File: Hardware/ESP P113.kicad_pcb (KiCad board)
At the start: 2 copper layers, 104.8 x 73.7 mm, 55 parts, among them J1 L_In, J2 R_In, J3 L_Out, J4 R_Out, J5 AC_In, Q1 MJE15032, Q2 MJE15033, Q3 MJE15032, Q4 MJE15033, U1 LM4562

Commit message: Updated to V1.1
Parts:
- added F1: Fuse_Small, Fuse:Fuseholder_Cylinder-5x20mm_Schurter_0031_8201_Horizontal_Open, F.Cu at (74.9, 62.2)
- added H5: MountingHole, MountingHole:MountingHole_3.2mm_M3_Pad_Via, F.Cu at (63.5, 29.8)
- J5: footprint TerminalBlock_Phoenix:TerminalBlock_Phoenix_MKDS-1,5-2_1x02_P5.00mm_Horizontal -> TerminalBlock_Phoenix:TerminalBlock_Phoenix_MKDS-1,5-2-5.08_1x02_P5.08mm_Horizontal
- L1, L2: footprint Inductor_SMD:L_Bourns_SRP1245A -> Inductor_THT:L_Radial_D12.5mm_P9.00mm_Fastron_09HCP
- moved H1 63.3 mm to (117.5, 62.2)
- moved R12 15.7 mm to (149.9, 76.8)
- moved R4 15.7 mm to (149.9, 47.6)
- moved L1 5.08 mm to (127.0, 29.2)
- moved R15 3.86 mm to (156.8, 79.4), turned to 180 degrees
- moved R8 3.86 mm to (156.8, 45.1), turned to 0 degrees
- moved L2 3.81 mm to (127.0, 86.4)
- moved J3 3.70 mm to (151.1, 40.6)
- moved Q1 3.18 mm to (157.5, 29.2)
- moved Q2 3.18 mm to (157.5, 49.5)
- moved Q3 3.18 mm to (157.5, 69.8)
- moved Q4 3.18 mm to (157.5, 90.2)
- moved J4 2.84 mm to (151.1, 81.3)
- moved H3 2.54 mm to (143.5, 36.8)
- moved H4 2.54 mm to (143.5, 87.6)
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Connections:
- J5 pad 1: Net-(J5-Pad1) -> Net-(F1-Pad1)
- PS1 pad 1: Net-(J5-Pad1) -> Net-(F1-Pad2)
- PS2 pad 1: Net-(J5-Pad1) -> Net-(F1-Pad2)
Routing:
- net Net-(F1-Pad2): track 0.00 -> 79.3 mm
- net Net-(J5-Pad1): track 47.5 -> 0.00 mm
- net Net-(C2-Pad1): track 36.3 -> 23.2 mm
- net Net-(F1-Pad1): track 0.00 -> 11.2 mm
- net Net-(C6-Pad1): track 32.8 -> 24.4 mm
- net +15: track 117.7 -> 111.1 mm
- net R_Out: track 20.3 -> 15.2 mm
- net Net-(C7-Pad2): track 48.4 -> 43.3 mm
- net Net-(Q2-Pad2): track 3.87 -> 8.43 mm
- net Net-(C14-Pad1): track 28.4 -> 23.9 mm
- net Net-(C8-Pad2): track 15.6 -> 11.9 mm
- net -15: track 145.3 -> 141.8 mm
- net Net-(C15-Pad2): track 26.4 -> 23.1 mm
- net Net-(C3-Pad2): track 43.1 -> 39.9 mm
- net Net-(C4-Pad2): track 14.8 -> 11.6 mm
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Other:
- board size 104.8 x 73.7 mm -> 101.6 x 72.4 mm
- board text added: "+"
- board text added: "-"
- board text added: "ESP P113 Layout by Aria V1.1"
- board text removed: "+ In"
- board text removed: "ESP Project 113 Layout by Aria V1.0"
- board text removed: "Out +"

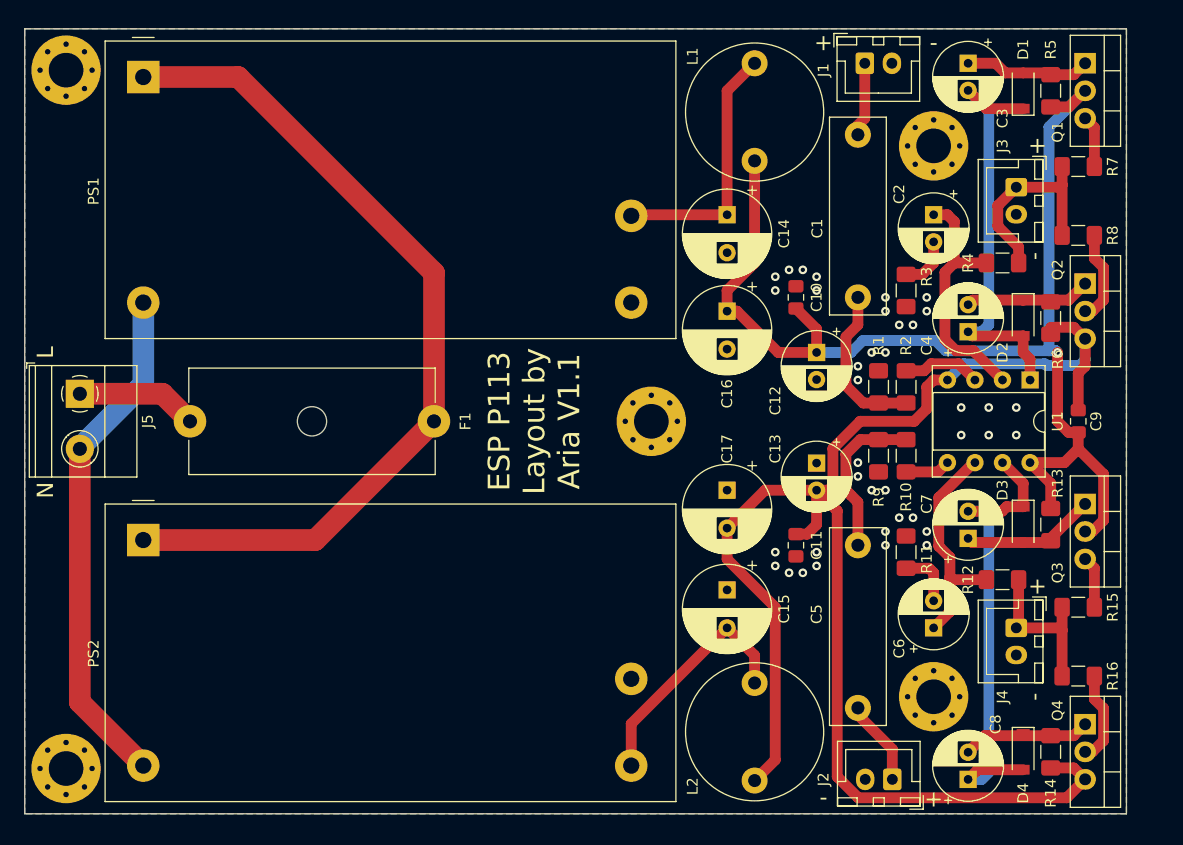
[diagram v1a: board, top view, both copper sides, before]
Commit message: Removed ground plane from PSU area
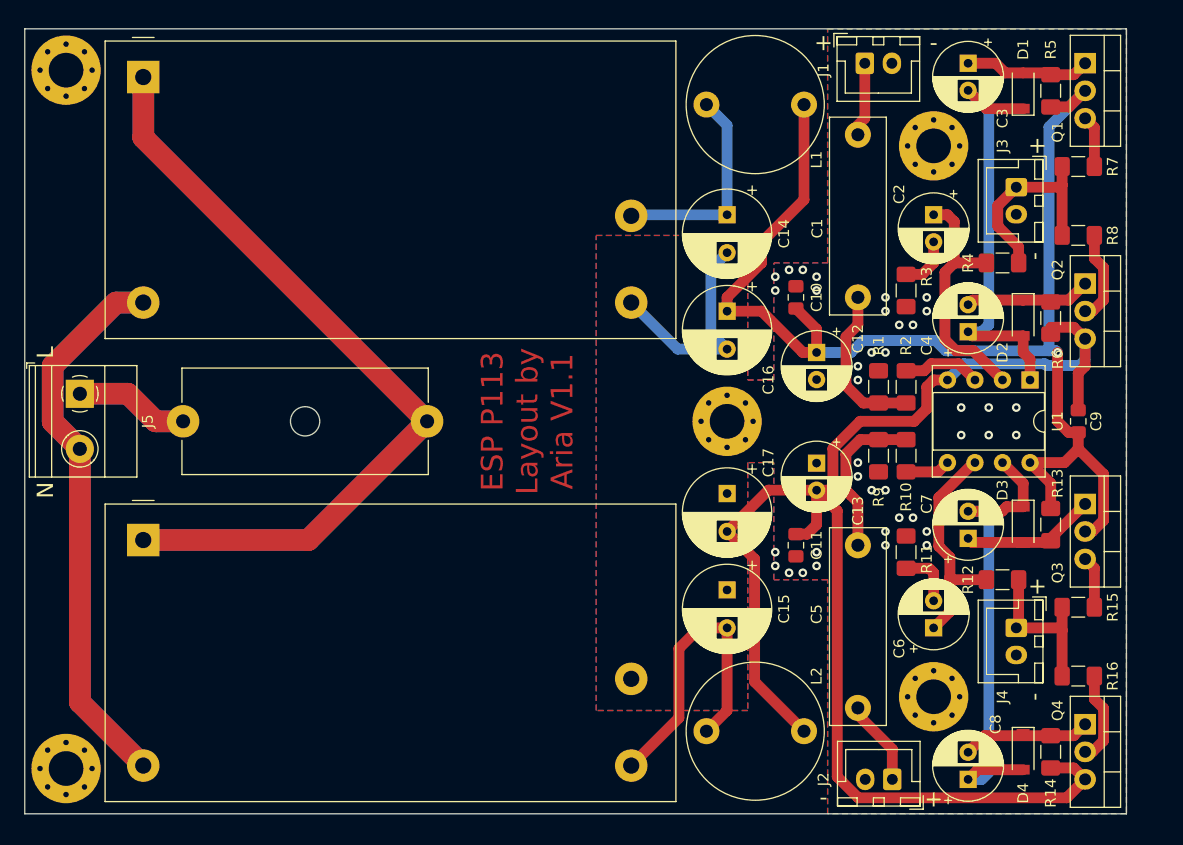
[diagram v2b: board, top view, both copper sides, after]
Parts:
- moved H1 6.98 mm to (124.5, 62.2)
- moved L2 6.29 mm to (122.6, 90.8), turned to 0 degrees
- moved L1 5.85 mm to (122.6, 33.0), turned to 0 degrees
- moved F1 0.64 mm to (74.3, 62.2)
- moved C17 0.31 mm to (124.5, 68.9)
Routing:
- net Net-(F1-Pad2): track 79.3 -> 146.6 mm
- net Net-(J5-Pad2): track 47.5 -> 102.2 mm
- net Earth: track 0.00 -> 20.7 mm
- net Net-(F1-Pad1): track 11.2 -> 21.2 mm
- net +15: track 111.1 -> 118.2 mm
- net Net-(C15-Pad2): track 23.1 -> 28.7 mm
- net -15: track 141.8 -> 137.3 mm
- net Net-(C14-Pad1): track 23.9 -> 19.8 mm

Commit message: Updated to V1.2.
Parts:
- added D5: LED, LED_THT:LED_D3.0mm, F.Cu at (123.2, 28.6)
- added D6: LED, LED_THT:LED_D3.0mm, F.Cu at (123.2, 95.9)
- added R17: 1k, Resistor_SMD:R_1206_3216Metric_Pad1.42x1.75mm_HandSolder, F.Cu at (129.5, 29.8)
- added R18: 1k, Resistor_SMD:R_1206_3216Metric_Pad1.42x1.75mm_HandSolder, F.Cu at (129.5, 94.6)
- C14, C15, C16, C17: value 330u -> 220u
- L1, L2: value 3u3 -> 4.7u; footprint Inductor_THT:L_Radial_D12.5mm_P9.00mm_Fastron_09HCP -> Inductor_SMD:L_Taiyo-Yuden_NR-80xx_HandSoldering
- moved L1 5.12 mm to (127.0, 35.6)
- moved L2 4.84 mm to (127.0, 88.9)
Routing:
- net Earth: track 20.7 -> 38.8 mm
- net Net-(C14-Pad1): track 19.8 -> 16.2 mm
- net Net-(C15-Pad2): track 28.7 -> 25.4 mm
- net Net-(D6-Pad2): track 0.00 -> 2.85 mm
- net Net-(D5-Pad2): track 0.00 -> 2.85 mm
- net -15: track 137.3 -> 139.7 mm
- net +15: track 118.2 -> 120.5 mm
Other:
- board size 101.6 x 72.4 mm -> 100.3 x 72.4 mm
- board text added: "ESP P113 Layout by Aria V1.2"
- board text removed: "ESP P113 Layout by Aria V1.1"
